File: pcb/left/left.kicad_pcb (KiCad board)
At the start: 2 copper layers, 163.5 x 132.8 mm, 66 parts

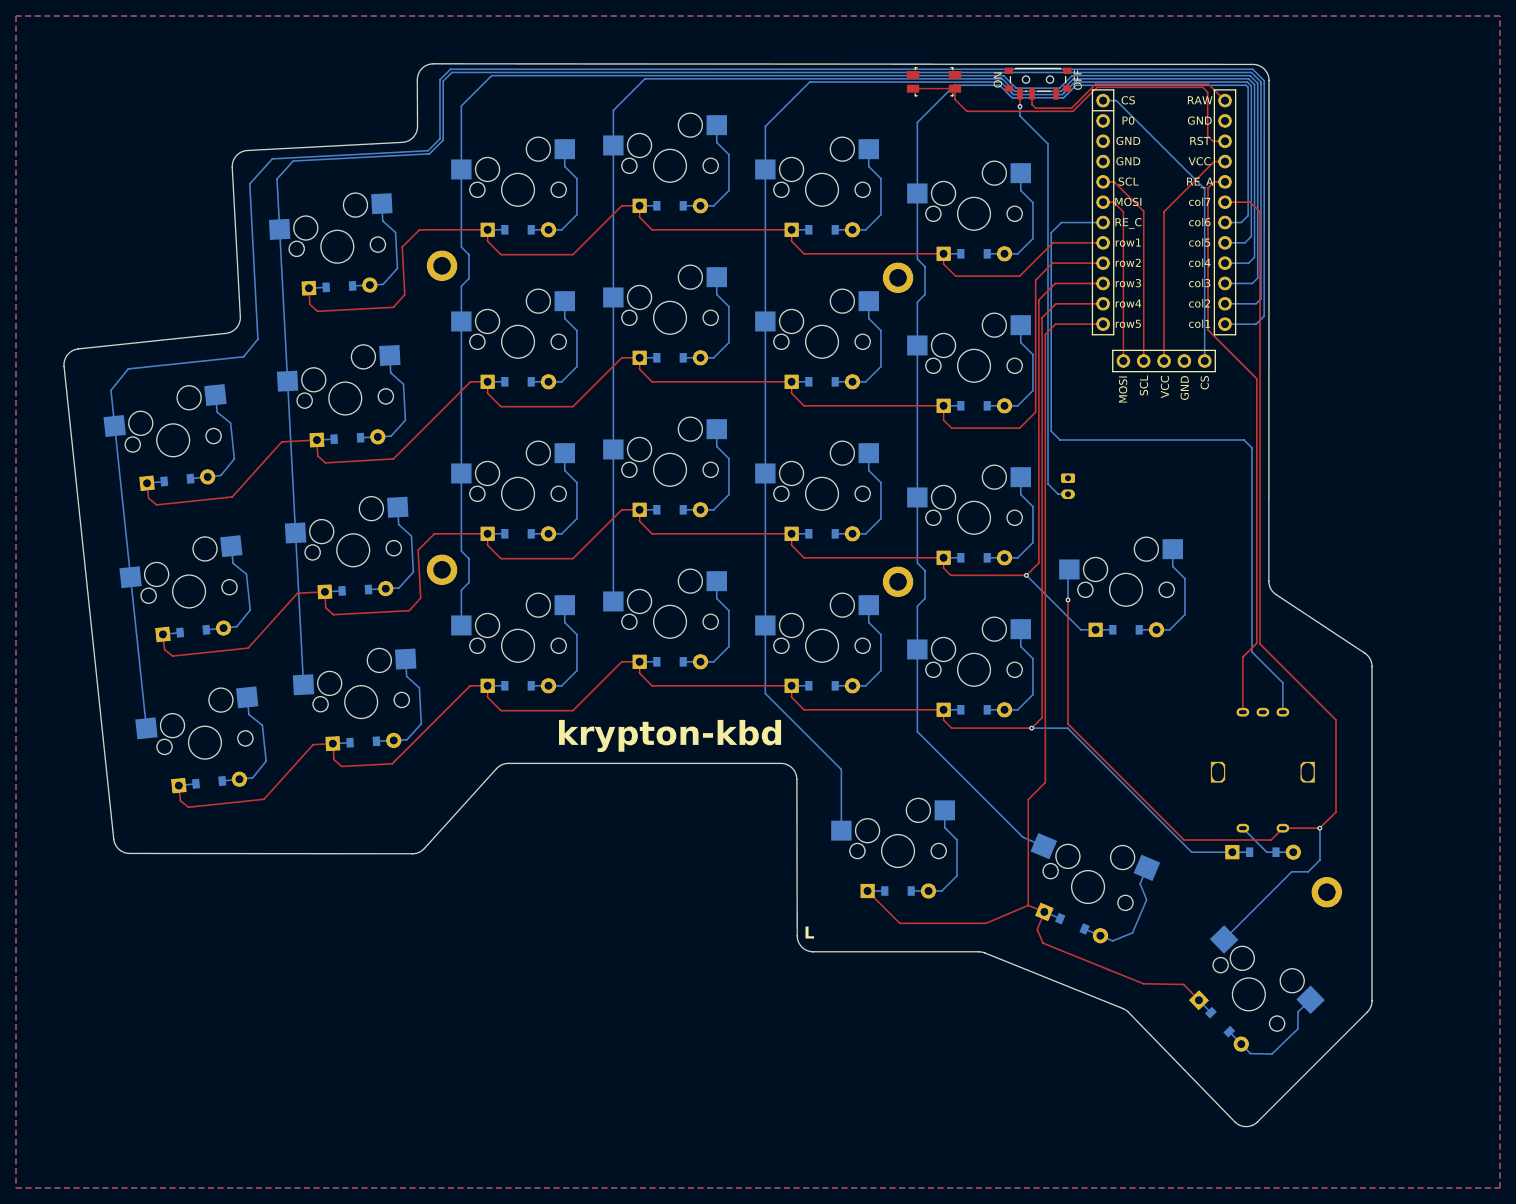
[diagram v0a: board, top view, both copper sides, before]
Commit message: Refined pcb routing, fixed hole issue on pcb
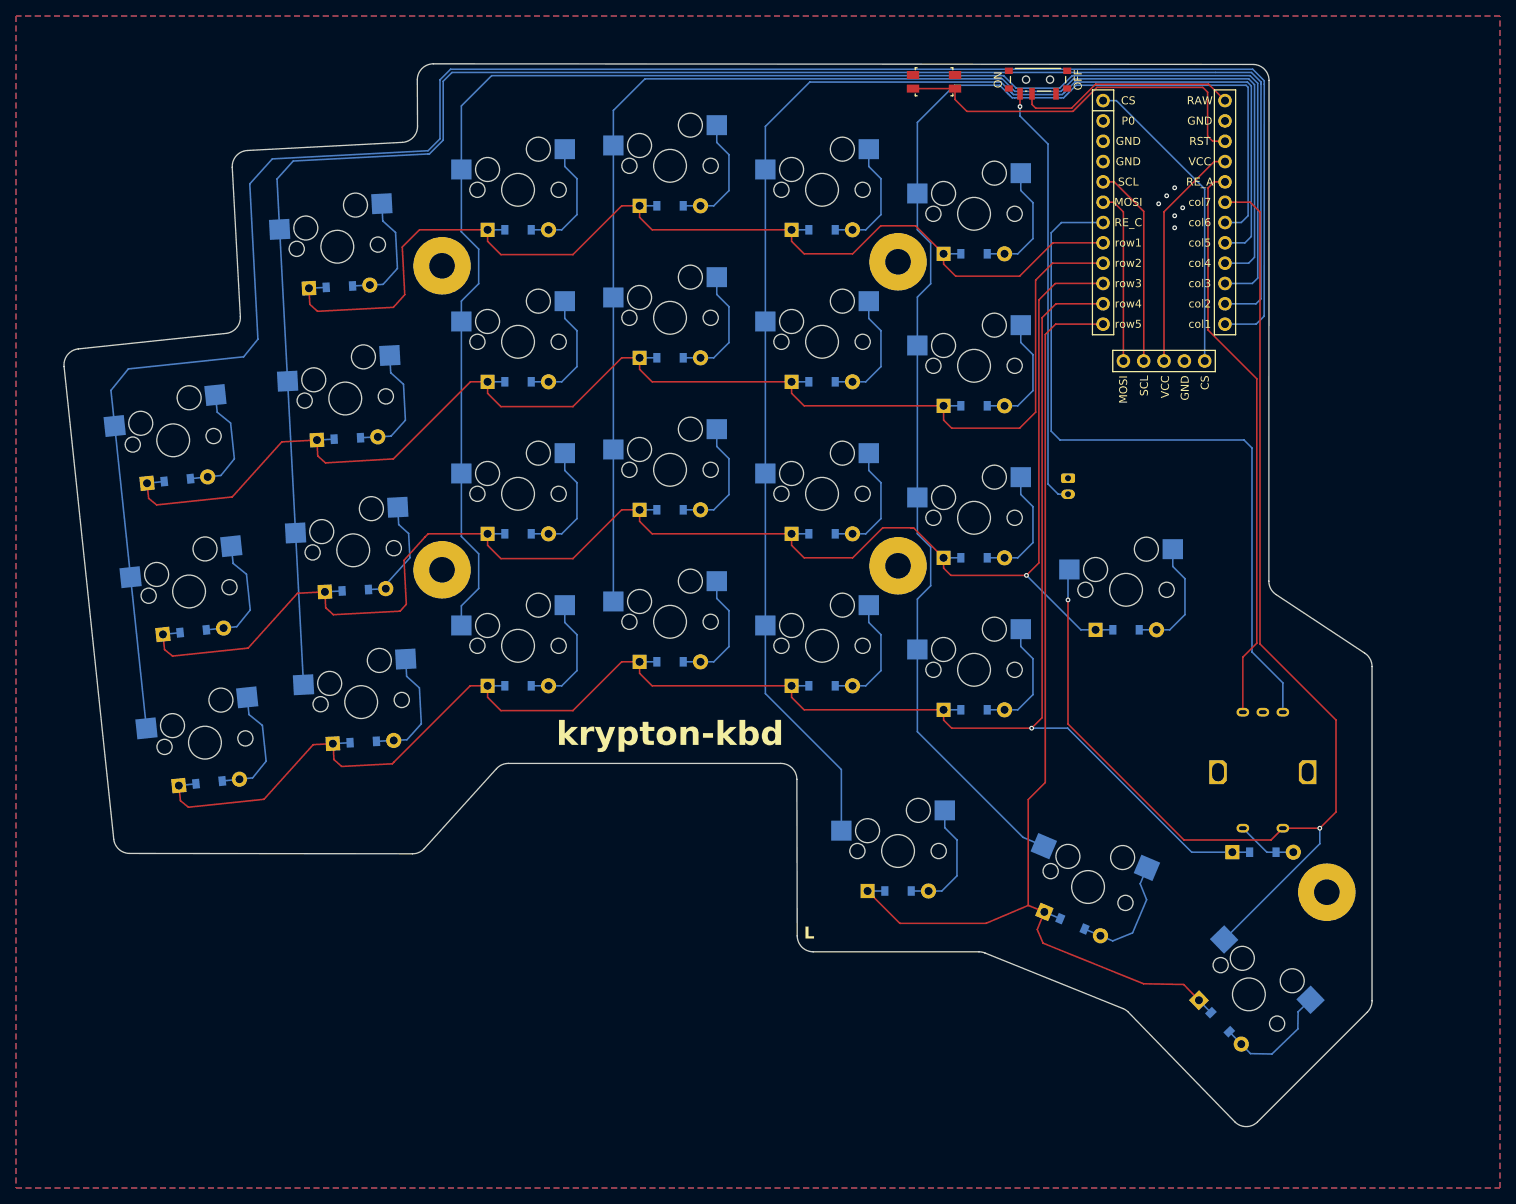
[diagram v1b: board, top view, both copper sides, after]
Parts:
- moved H3 2.00 mm to (220.4, 99.0)
- moved H4 2.00 mm to (220.4, 137.0)
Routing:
- net row1: track 132.6 -> 135.9 mm
- net row3: track 204.2 -> 207.3 mm
- net col3: track 198.0 -> 200.1 mm
- net pinky_home: track 15.3 -> 14.1 mm
- net col7: track 164.2 -> 163.0 mm
- net col6: track 163.2 -> 164.4 mm
- net GND: vias 0 -> 6
